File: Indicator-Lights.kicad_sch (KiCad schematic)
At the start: 7 parts, among them Q18 SI2347DS-T1-GE3, Q19 SI2347DS-T1-GE3

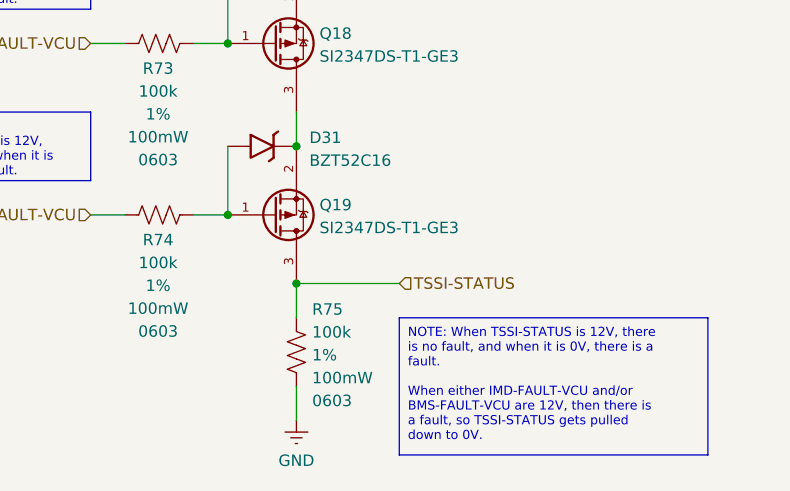
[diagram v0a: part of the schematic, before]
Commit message: updated port directionalities, updated pinout
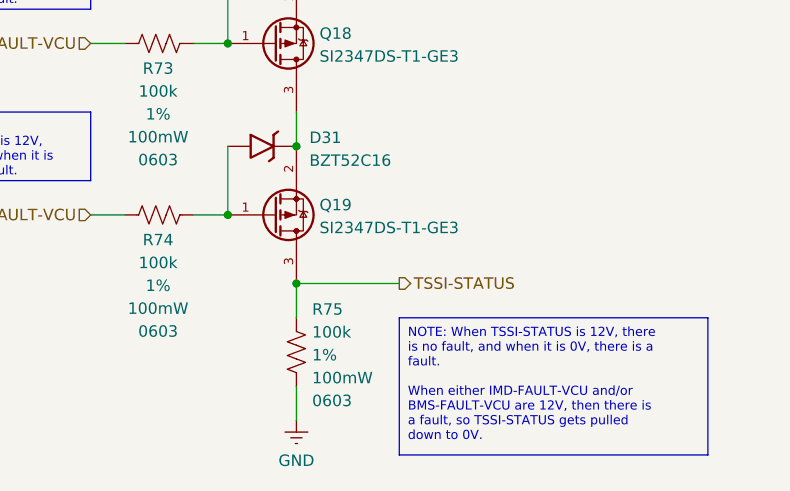
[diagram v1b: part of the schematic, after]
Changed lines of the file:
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@@
 	)
 	(hierarchical_label "TSSI-STATUS"
-		(shape input)
+		(shape output)
 		(at 220.98 156.21 0)
 		(effects

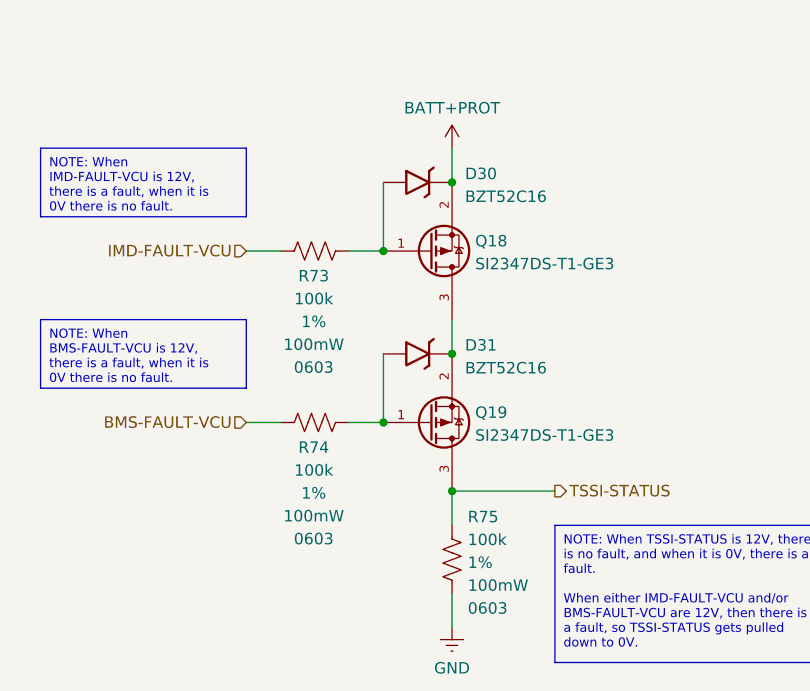
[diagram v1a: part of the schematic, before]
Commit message: Schem is reannotated time to redo all of the layout
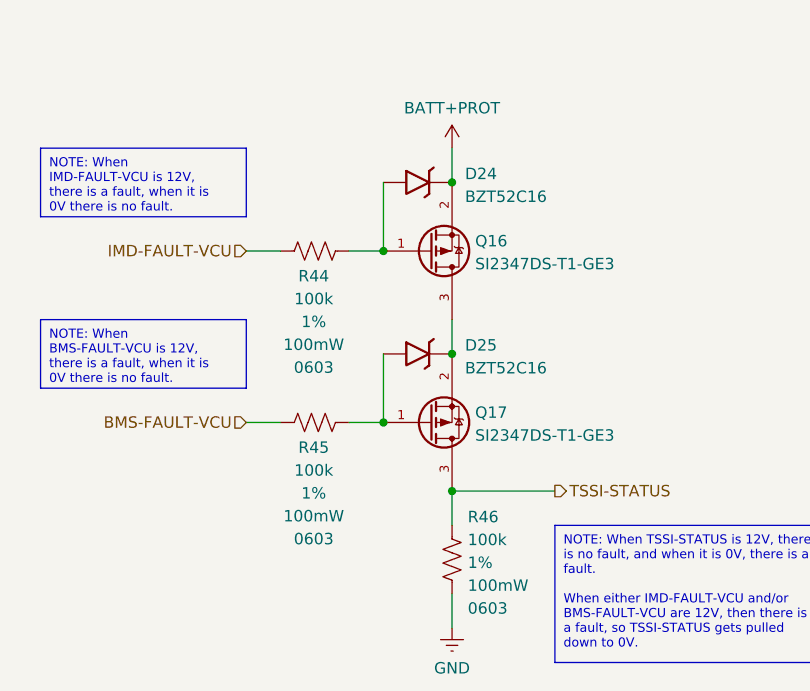
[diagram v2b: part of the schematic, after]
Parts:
- renumbered D30 to D24, D31 to D25, Q18 to Q16, Q19 to Q17, R73 to R44, R74 to R45, R75 to R46
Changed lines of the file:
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@@
 		(on_board yes)
 		(dnp no)
-		(property "Reference" "D31"
+		(property "Reference" "D25"
 			(at 210.9881 140.0119 0)
 			(effects
@@
 			(project "Shutdown"
 				(path "/624b8e71-6fec-49ba-b7c9-b659e140fc2f/42f0cf19-0e14-403a-bef6-1dfa2279046f"
-					(reference "D31")
+					(reference "D25")
 					(unit 1)
 				)
@@
 		(on_board yes)
 		(dnp no)
-		(property "Reference" "#PWR084"
+		(property "Reference" "#PWR043"
 			(at 209.55 121.92 0)
 			(effects
@@
 			(project "Shutdown"
 				(path "/624b8e71-6fec-49ba-b7c9-b659e140fc2f/42f0cf19-0e14-403a-bef6-1dfa2279046f"
-					(reference "#PWR084")
+					(reference "#PWR043")
 					(unit 1)
 				)
@@
 		(on_board yes)
 		(dnp no)
-		(property "Reference" "R73"
+		(property "Reference" "R44"
 			(at 194.184 132.3247 0)
 			(effects
@@
 			(project "Shutdown"
 				(path "/624b8e71-6fec-49ba-b7c9-b659e140fc2f/42f0cf19-0e14-403a-bef6-1dfa2279046f"
-					(reference "R73")
+					(reference "R44")
 					(unit 1)
 				)
@@
 		(on_board yes)
 		(dnp no)
-		(property "Reference" "Q19"
+		(property "Reference" "Q17"
 			(at 212.1133 147.4882 0)
 			(effects
@@
 			(project "Shutdown"
 				(path "/624b8e71-6fec-49ba-b7c9-b659e140fc2f/42f0cf19-0e14-403a-bef6-1dfa2279046f"
-					(reference "Q19")
+					(reference "Q17")
 					(unit 1)
 				)
@@
 		(on_board yes)
 		(dnp no)
-		(property "Reference" "Q18"
+		(property "Reference" "Q16"
 			(at 212.1133 128.4382 0)
 			(effects
@@
 			(project ""
 				(path "/624b8e71-6fec-49ba-b7c9-b659e140fc2f/42f0cf19-0e14-403a-bef6-1dfa2279046f"
-					(reference "Q18")
+					(reference "Q16")
 					(unit 1)
 				)
@@
 		(on_board yes)
 		(dnp no)
-		(property "Reference" "#PWR085"
+		(property "Reference" "#PWR044"
 			(at 209.55 177.8 0)
 			(effects
@@
 			(project "Shutdown"
 				(path "/624b8e71-6fec-49ba-b7c9-b659e140fc2f/42f0cf19-0e14-403a-bef6-1dfa2279046f"
-					(reference "#PWR085")
+					(reference "#PWR044")
 					(unit 1)
 				)
@@
 		(on_board yes)
 		(dnp no)
-		(property "Reference" "R75"
+		(property "Reference" "R46"
 			(at 211.2951 159.088 90)
 			(effects
@@
 			(project "Shutdown"
 				(path "/624b8e71-6fec-49ba-b7c9-b659e140fc2f/42f0cf19-0e14-403a-bef6-1dfa2279046f"
-					(reference "R75")
+					(reference "R46")
 					(unit 1)
 				)
@@
 		(on_board yes)
 		(dnp no)
-		(property "Reference" "D30"
+		(property "Reference" "D24"
 			(at 210.9881 120.9619 0)
 			(effects
@@
 			(project ""
 				(path "/624b8e71-6fec-49ba-b7c9-b659e140fc2f/42f0cf19-0e14-403a-bef6-1dfa2279046f"
-					(reference "D30")
+					(reference "D24")
 					(unit 1)
 				)
@@
 		(on_board yes)
 		(dnp no)
-		(property "Reference" "R74"
+		(property "Reference" "R45"
 			(at 194.184 151.3747 0)
 			(effects
@@
 			(project "Shutdown"
 				(path "/624b8e71-6fec-49ba-b7c9-b659e140fc2f/42f0cf19-0e14-403a-bef6-1dfa2279046f"
-					(reference "R74")
+					(reference "R45")
 					(unit 1)
 				)

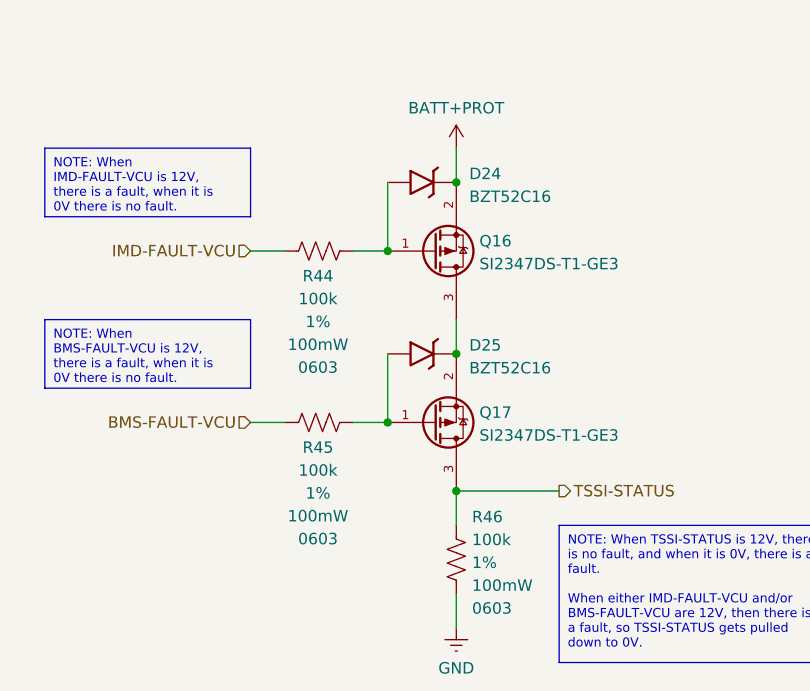
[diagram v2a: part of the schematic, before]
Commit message: Finished shutdown, 0 drc, need to export gerbers
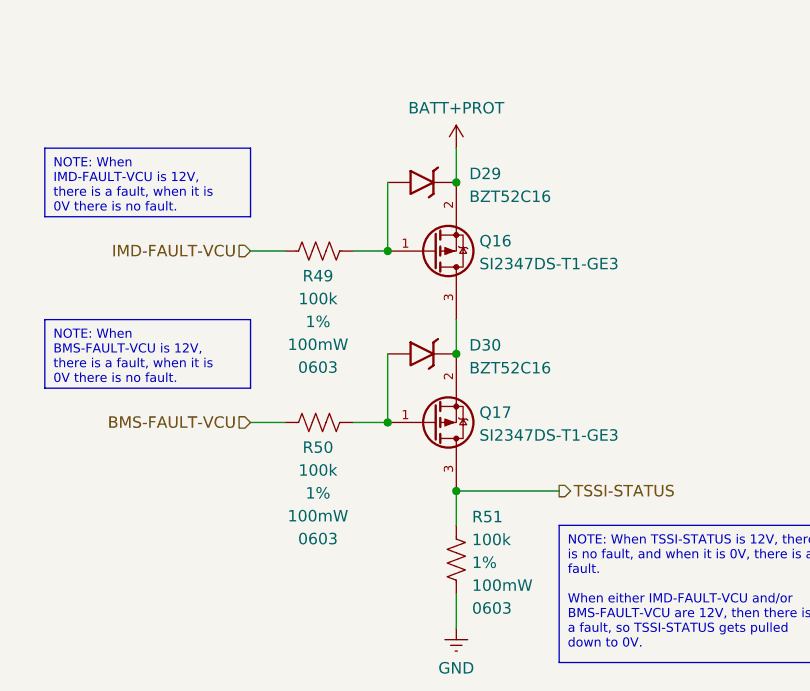
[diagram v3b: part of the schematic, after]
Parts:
- renumbered D24 to D29, D25 to D30, R44 to R49, R45 to R50, R46 to R51
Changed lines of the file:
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@@
 		(on_board yes)
 		(dnp no)
-		(property "Reference" "D25"
+		(property "Reference" "D30"
 			(at 210.9881 140.0119 0)
 			(effects
@@
 			(project "Shutdown"
 				(path "/624b8e71-6fec-49ba-b7c9-b659e140fc2f/42f0cf19-0e14-403a-bef6-1dfa2279046f"
-					(reference "D25")
+					(reference "D30")
 					(unit 1)
 				)
@@
 		(on_board yes)
 		(dnp no)
-		(property "Reference" "#PWR043"
+		(property "Reference" "#PWR048"
 			(at 209.55 121.92 0)
 			(effects
@@
 			(project "Shutdown"
 				(path "/624b8e71-6fec-49ba-b7c9-b659e140fc2f/42f0cf19-0e14-403a-bef6-1dfa2279046f"
-					(reference "#PWR043")
+					(reference "#PWR048")
 					(unit 1)
 				)
@@
 		(on_board yes)
 		(dnp no)
-		(property "Reference" "R44"
+		(property "Reference" "R49"
 			(at 194.184 132.3247 0)
 			(effects
@@
 			(project "Shutdown"
 				(path "/624b8e71-6fec-49ba-b7c9-b659e140fc2f/42f0cf19-0e14-403a-bef6-1dfa2279046f"
-					(reference "R44")
+					(reference "R49")
 					(unit 1)
 				)
@@
 		(on_board yes)
 		(dnp no)
-		(property "Reference" "#PWR044"
+		(property "Reference" "#PWR049"
 			(at 209.55 177.8 0)
 			(effects
@@
 			(project "Shutdown"
 				(path "/624b8e71-6fec-49ba-b7c9-b659e140fc2f/42f0cf19-0e14-403a-bef6-1dfa2279046f"
-					(reference "#PWR044")
+					(reference "#PWR049")
 					(unit 1)
 				)
@@
 		(on_board yes)
 		(dnp no)
-		(property "Reference" "R46"
+		(property "Reference" "R51"
 			(at 211.2951 159.088 90)
 			(effects
@@
 			(project "Shutdown"
 				(path "/624b8e71-6fec-49ba-b7c9-b659e140fc2f/42f0cf19-0e14-403a-bef6-1dfa2279046f"
-					(reference "R46")
+					(reference "R51")
 					(unit 1)
 				)
@@
 		(on_board yes)
 		(dnp no)
-		(property "Reference" "D24"
+		(property "Reference" "D29"
 			(at 210.9881 120.9619 0)
 			(effects
@@
 			(project ""
 				(path "/624b8e71-6fec-49ba-b7c9-b659e140fc2f/42f0cf19-0e14-403a-bef6-1dfa2279046f"
-					(reference "D24")
+					(reference "D29")
 					(unit 1)
 				)
@@
 		(on_board yes)
 		(dnp no)
-		(property "Reference" "R45"
+		(property "Reference" "R50"
 			(at 194.184 151.3747 0)
 			(effects
@@
 			(project "Shutdown"
 				(path "/624b8e71-6fec-49ba-b7c9-b659e140fc2f/42f0cf19-0e14-403a-bef6-1dfa2279046f"
-					(reference "R45")
+					(reference "R50")
 					(unit 1)
 				)

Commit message: schematic updated to V2 extra crispy
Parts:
- removed R51: 100k, Resistor_SMD:R_0603_1608Metric_Pad0.98x0.95mm_HandSolder, symbol -R-SMD-0603:R-0603-100k-1%-100mW-100PPM
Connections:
- net TSSI-STATUS is gone; now on net GND: Q17.3 (D)
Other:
- moved on the sheet: D29, D30, Q16, Q17, R49, R50
